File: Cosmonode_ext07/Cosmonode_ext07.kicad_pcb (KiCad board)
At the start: 2 copper layers, 37.5 x 34.3 mm, 9 parts, among them J1 OSHW_Logo, J2 MH-Z19, J3 CONN_01X08, J4 CONN_01X08, J5 GS3, J6 GS3, J7 Aloes_Logo, J8 CONN_01X09, U1 XC6206P502MR

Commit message: fully update to v0.3
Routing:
- net Net-(J2-Pad7): track 2.43 -> 46.7 mm, vias 1 -> 0
- net GND: track 49.2 -> 23.1 mm
- net +3V3: track 37.6 -> 44.6 mm
- net /TX: track 9.52 -> 11.0 mm
- net /AREF: track 27.8 -> 26.3 mm
- net +5V: track 21.7 -> 23.0 mm
- added copper zone on B.Cu, net GND
- added copper zone on F.Cu, net GND
- removed copper zone on B.Cu, net Net-(J2-Pad7)
- removed copper zone on F.Cu, net Net-(J2-Pad7)
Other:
- outline, holes or cut-outs redrawn

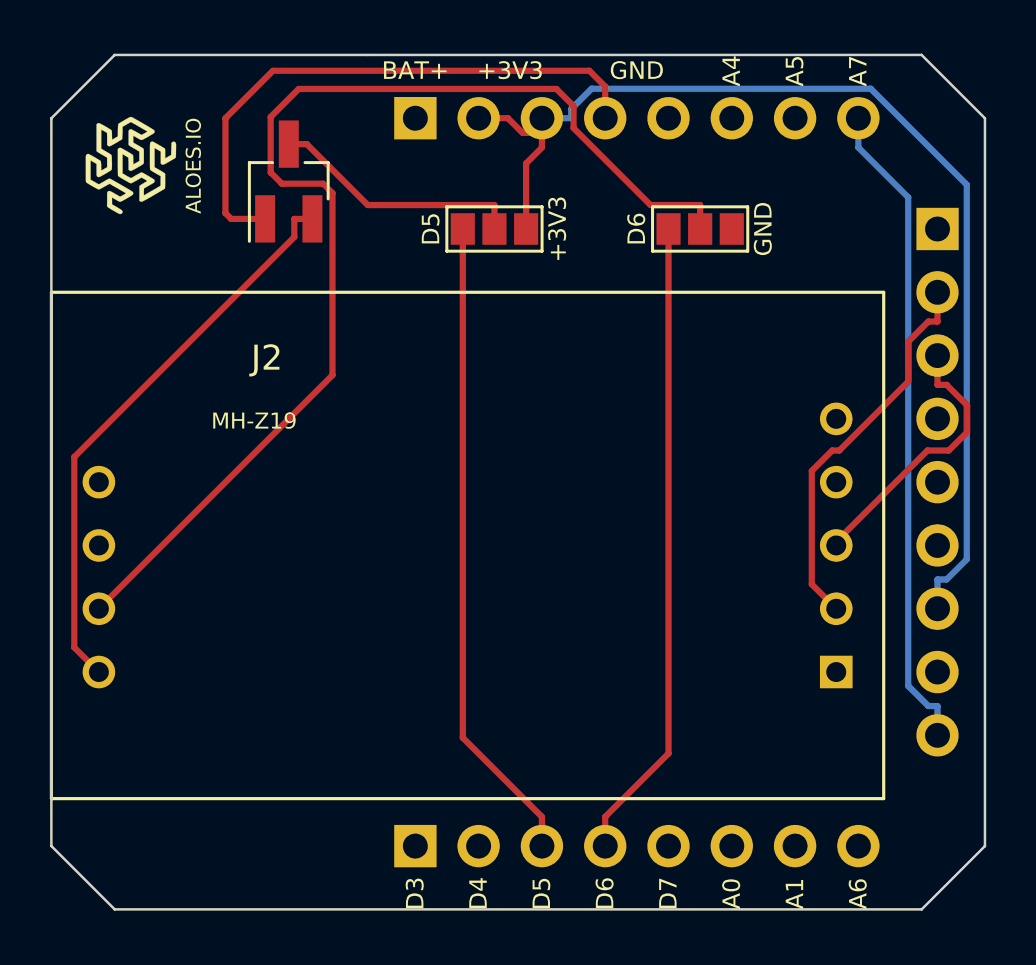
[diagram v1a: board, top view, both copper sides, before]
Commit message: update to v0.5 ( base, ext05, ext07, ext08 )
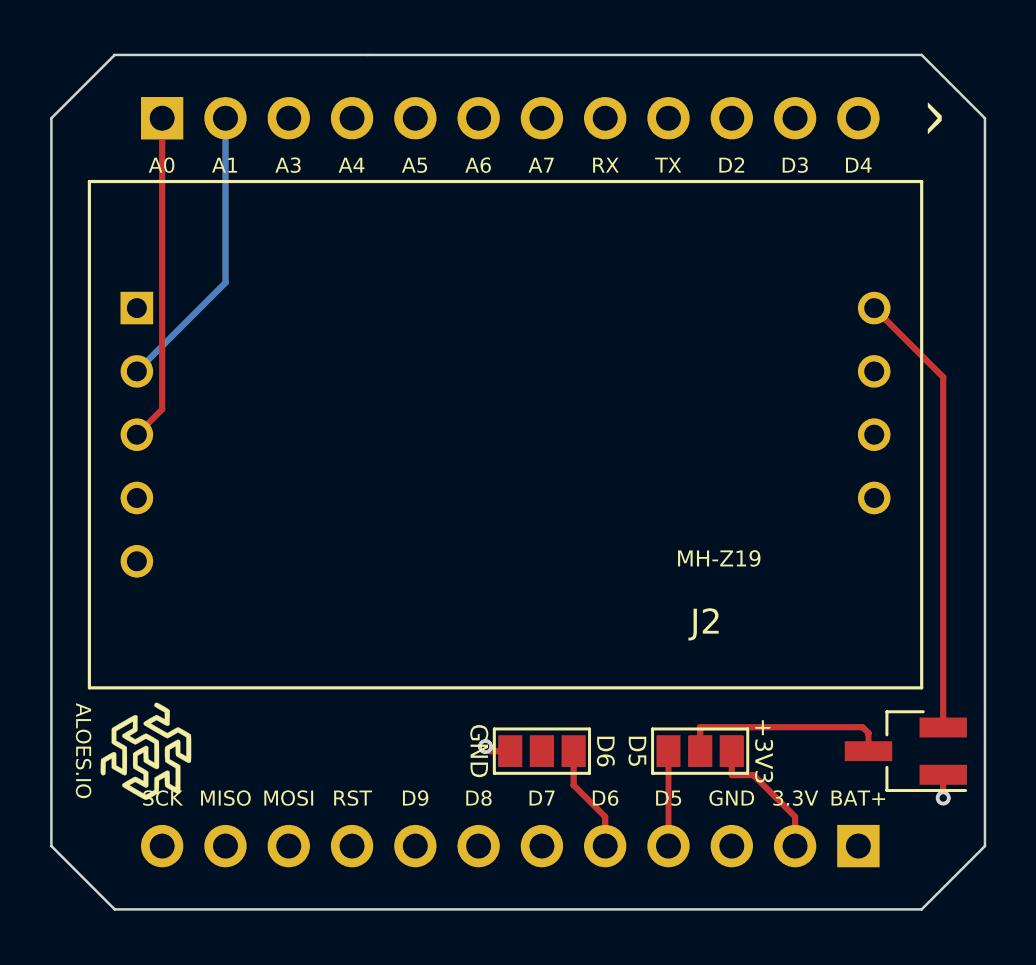
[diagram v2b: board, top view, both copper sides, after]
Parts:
- removed J8: CONN_01X09, Pin_Headers:Pin_Header_Straight_1x09_Pitch2.54mm
- J3, J4: value CONN_01X08 -> CONN_01X12; footprint Pin_Headers:Pin_Header_Straight_1x08_Pitch2.54mm -> Pin_Headers:Pin_Header_Straight_1x12_Pitch2.54mm
- moved J2 34.4 mm to (177.2, 99.1), turned to 180 degrees
- moved J4 34.2 mm to (176.5, 120.7), turned to 90 degrees
- moved U1 33.7 mm to (178.4, 116.8), turned to 180 degrees
- moved J3 30.9 mm to (148.6, 91.4)
- moved J7 23.5 mm to (148.0, 116.8), turned to 270 degrees
- moved J5 22.5 mm to (170.2, 116.8)
- moved J6 21.9 mm to (163.8, 116.8), turned to 270 degrees
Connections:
- net /A0 renamed A6
- net /A1 renamed A7
- net /A4 renamed D7
- net /A5 renamed D8
- net /A6 renamed RX
- net /BAT+ renamed +BATT
- net /D7 renamed A5
- J2 pad 2: /RX -> A1
- J2 pad 3: /TX -> A0
- J2 pad 7: Net-(J2-Pad7) -> GND
- J3 pad 1: /D3 -> A0
- J3 pad 2: /D4 -> A1
- J3 pad 3: /D5 -> A3
- J3 pad 4: /D6 -> A4
- J4 pad 3: +3V3 -> GND
- J4 pad 4: GND -> D5
- J4 pad 5: GND -> D6
- J4 pad 8: /AREF -> D9
- J5 pad 1: /D5 -> D5
- J6 pad 1: /D6 -> D6
- J6 pad 2: Net-(J2-Pad7) -> Net-(J6-Pad2)
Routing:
- net Net-(J2-Pad7): track 46.7 -> 0.00 mm
- net +3V3: track 44.6 -> 5.37 mm
- net /AREF: track 26.3 -> 0.00 mm
- net /D5: track 26.1 -> 0.00 mm
- net /D6: track 25.8 -> 0.00 mm
- net GND: track 23.1 -> 2.00 mm, vias 0 -> 2
- net /RX: track 15.6 -> 0.00 mm
- net A0: track 0.00 -> 13.1 mm
- net A1: track 0.00 -> 11.6 mm
- net /TX: track 11.0 -> 0.00 mm
- net +5V: track 23.0 -> 18.0 mm
- net D6: track 0.00 -> 4.34 mm
- net D5: track 0.00 -> 3.81 mm
- net Net-(J5-Pad2): track 10.2 -> 8.54 mm
- removed copper zone on F.Cu, net GND
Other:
- board text added: "3.3V"
- board text added: "A3"
- board text added: "D2"
- board text added: "D8"
- board text added: "D9"
- board text added: "MISO"
- board text added: "MOSI"
- board text added: "RST"
- board text added: "RX"
- board text added: "SCK"
- board text added: "TX"
- board text added: "^"

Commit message: update to V0.7 (WIP)
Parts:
- moved J7 2.01 mm to (149.9, 116.2)
- moved U1 2.01 mm to (176.5, 116.2)
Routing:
- net GND: track 2.00 -> 40.0 mm, vias 2 -> 0
- net Net-(J5-Pad2): track 8.54 -> 5.95 mm
- net Net-(J6-Pad2): track 0.00 -> 1.15 mm, vias 0 -> 1
- net +5V: track 18.0 -> 17.1 mm
- added copper zone on B.Cu, net Net-(J6-Pad2)
- removed copper zone on B.Cu, net GND
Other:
- board size 37.5 x 34.3 mm -> 34.3 x 34.3 mm
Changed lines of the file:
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@@
-(kicad_pcb (version 4) (host pcbnew 4.0.7-e2-6376~58~ubuntu17.04.1)
+(kicad_pcb (version 4) (host pcbnew 4.0.7-e2-6376~60~ubuntu17.10.1)
   (general
     (links 10)
     (no_connects 0)
-    (area 144.094999 88.849999 181.660001 123.240001)
+    (area 145.364999 88.849999 179.755001 123.240001)
     (thickness 1.6)
     (drawings 42)
-    (tracks 23)
+    (tracks 45)
     (zones 0)
     (modules 8)
@@
   )
   (module Aloes:Aloes_mini (layer F.Cu)
-    (at 147.955 116.84 270)
+    (at 149.86 116.205 270)
     (fp_text reference J7 (at 0 0 270) (layer F.SilkS) hide
       (effects (font (thickness 0.3)))
@@
   )
   (module TO_SOT_Packages_SMD:SOT-23_Handsoldering (layer F.Cu)
-    (at 178.435 116.84 180)
+    (at 176.53 116.205 180)
     (descr "SOT-23, Handsoldering")
     (tags SOT-23)
@@
     )
   )
-  (gr_text ^ (at 179.07 91.44 270) (layer F.SilkS)
+  (gr_line (start 147.955 123.19) (end 177.165 123.19) (angle 90) (layer Edge.Cuts) (width 0.1))
+  (gr_line (start 147.955 88.9) (end 156.845 88.9) (angle 90) (layer Edge.Cuts) (width 0.1))
+  (gr_line (start 145.415 120.65) (end 147.955 123.19) (angle 90) (layer Edge.Cuts) (width 0.1))
+  (gr_line (start 145.415 91.44) (end 145.415 120.65) (angle 90) (layer Edge.Cuts) (width 0.1))
+  (gr_line (start 147.955 88.9) (end 145.415 91.44) (angle 90) (layer Edge.Cuts) (width 0.1))
+  (gr_line (start 156.845 88.9) (end 177.165 88.9) (angle 90) (layer Edge.Cuts) (width 0.1))
+  (gr_line (start 179.705 91.44) (end 177.165 88.9) (angle 90) (layer Edge.Cuts) (width 0.1))
+  (gr_line (start 179.705 120.65) (end 179.705 91.44) (angle 90) (layer Edge.Cuts) (width 0.1))
+  (gr_line (start 177.165 123.19) (end 179.705 120.65) (angle 90) (layer Edge.Cuts) (width 0.1))
+  (gr_text ^ (at 177.8 91.44 270) (layer F.SilkS)
     (effects (font (size 1.5 1.5) (thickness 0.3)))
   )
@@
     (effects (font (size 0.6 0.6) (thickness 0.1)))
   )
-  (gr_line (start 179.07 123.19) (end 146.685 123.19) (angle 90) (layer Edge.Cuts) (width 0.1))
-  (gr_line (start 181.61 91.44) (end 181.61 120.65) (angle 90) (layer Edge.Cuts) (width 0.1))
-  (gr_line (start 156.845 88.9) (end 179.07 88.9) (angle 90) (layer Edge.Cuts) (width 0.1))
-  (gr_line (start 181.61 120.65) (end 179.07 123.19) (angle 90) (layer Edge.Cuts) (width 0.1))
-  (gr_line (start 179.07 88.9) (end 181.61 91.44) (angle 90) (layer Edge.Cuts) (width 0.1))
   (gr_text GND (at 161.29 116.84 270) (layer F.SilkS)
     (effects (font (size 0.7 0.7) (thickness 0.1)))
@@
     (effects (font (size 0.7 0.7) (thickness 0.1)) (justify mirror))
   )
-  (gr_line (start 146.685 88.9) (end 156.845 88.9) (angle 90) (layer Edge.Cuts) (width 0.1))
-  (gr_line (start 144.145 91.44) (end 146.685 88.9) (angle 90) (layer Edge.Cuts) (width 0.1))
-  (gr_line (start 144.145 120.65) (end 144.145 91.44) (angle 90) (layer Edge.Cuts) (width 0.1))
-  (gr_line (start 146.685 123.19) (end 144.145 120.65) (angle 90) (layer Edge.Cuts) (width 0.1))
   (dimension 24.13 (width 0.3) (layer F.Fab)
     (gr_text "24,130 mm" (at 166.37 79.295) (layer F.Fab)
@@
     (arrow2b (pts (xy 154.305 80.645) (xy 155.431504 80.058579)))
   )
-  (gr_text ALOES.IO (at 145.415 116.84 270) (layer F.SilkS)
+  (gr_text ALOES.IO (at 147.32 116.205 270) (layer F.SilkS)
     (effects (font (size 0.6 0.6) (thickness 0.1)))
   )
@@
     (arrow2b (pts (xy 188.595 89.535) (xy 189.181421 90.661504)))
   )
-  (segment (start 179.935 101.83) (end 177.165 99.06) (width 0.25) (layer F.Cu) (net 1))
-  (segment (start 179.935 115.89) (end 179.935 101.83) (width 0.25) (layer F.Cu) (net 1))
+  (segment (start 178.6386 100.5336) (end 177.165 99.06) (width 0.25) (layer F.Cu) (net 1))
+  (segment (start 178.6386 113.9211) (end 178.6386 100.5336) (width 0.25) (layer F.Cu) (net 1))
+  (segment (start 178.03 114.5297) (end 178.6386 113.9211) (width 0.25) (layer F.Cu) (net 1))
+  (segment (start 178.03 115.255) (end 178.03 114.5297) (width 0.25) (layer F.Cu) (net 1))
   (segment (start 172.3156 117.8003) (end 171.45 117.8003) (width 0.25) (layer F.Cu) (net 2))
   (segment (start 173.99 119.4747) (end 172.3156 117.8003) (width 0.25) (layer F.Cu) (net 2))
   (segment (start 173.99 120.65) (end 173.99 119.4747) (width 0.25) (layer F.Cu) (net 2))
   (segment (start 171.45 116.84) (end 171.45 117.8003) (width 0.25) (layer F.Cu) (net 2))
-  (via (at 179.935 118.7207) (size 0.6) (layers F.Cu B.Cu) (net 3))
-  (via (at 161.5658 116.6561) (size 0.6) (layers F.Cu B.Cu) (net 3))
-  (segment (start 179.935 118.7207) (end 179.935 117.79) (width 0.25) (layer F.Cu) (net 3))
-  (segment (start 162.56 116.84) (end 161.7497 116.84) (width 0.25) (layer F.Cu) (net 3))
-  (segment (start 161.5658 116.6561) (end 161.7497 116.84) (width 0.25) (layer F.Cu) (net 3))
-  (segment (start 176.7 115.8797) (end 170.18 115.8797) (width 0.25) (layer F.Cu) (net 4))
-  (segment (start 176.935 116.1147) (end 176.7 115.8797) (width 0.25) (layer F.Cu) (net 4))
-  (segment (start 176.935 116.84) (end 176.935 116.1147) (width 0.25) (layer F.Cu) (net 4))
+  (segment (start 175.3546 118.5551) (end 176.7547 117.155) (width 0.25) (layer F.Cu) (net 3))
+  (segment (start 175.3546 120.9818) (end 175.3546 118.5551) (width 0.25) (layer F.Cu) (net 3))
+  (segment (start 174.4656 121.8708) (end 175.3546 120.9818) (width 0.25) (layer F.Cu) (net 3))
+  (segment (start 173.4788 121.8708) (end 174.4656 121.8708) (width 0.25) (layer F.Cu) (net 3))
+  (segment (start 172.6253 121.0173) (end 173.4788 121.8708) (width 0.25) (layer F.Cu) (net 3))
+  (segment (start 172.6253 120.65) (end 172.6253 121.0173) (width 0.25) (layer F.Cu) (net 3))
+  (segment (start 172.0377 120.65) (end 172.6253 120.65) (width 0.25) (layer F.Cu) (net 3))
+  (segment (start 178.03 117.155) (end 176.8673 117.155) (width 0.25) (layer F.Cu) (net 3))
+  (segment (start 176.8673 117.155) (end 176.7547 117.155) (width 0.25) (layer F.Cu) (net 3))
+  (segment (start 178.1882 102.6232) (end 177.165 101.6) (width 0.25) (layer F.Cu) (net 3))
+  (segment (start 178.1882 108.8937) (end 178.1882 102.6232) (width 0.25) (layer F.Cu) (net 3))
+  (segment (start 176.7547 110.3272) (end 178.1882 108.8937) (width 0.25) (layer F.Cu) (net 3))
+  (segment (start 176.7547 117.155) (end 176.7547 110.3272) (width 0.25) (layer F.Cu) (net 3))
+  (segment (start 162.56 116.84) (end 162.56 117.8003) (width 0.25) (layer F.Cu) (net 3))
+  (segment (start 172.0377 120.65) (end 171.45 120.65) (width 0.25) (layer F.Cu) (net 3))
+  (segment (start 162.6455 117.8003) (end 162.56 117.8003) (width 0.25) (layer F.Cu) (net 3))
+  (segment (start 165.1002 120.255) (end 162.6455 117.8003) (width 0.25) (layer F.Cu) (net 3))
+  (segment (start 165.1002 121.0828) (end 165.1002 120.255) (width 0.25) (layer F.Cu) (net 3))
+  (segment (start 165.8659 121.8485) (end 165.1002 121.0828) (width 0.25) (layer F.Cu) (net 3))
+  (segment (start 169.4435 121.8485) (end 165.8659 121.8485) (width 0.25) (layer F.Cu) (net 3))
+  (segment (start 170.2747 121.0173) (end 169.4435 121.8485) (width 0.25) (layer F.Cu) (net 3))
+  (segment (start 170.2747 120.65) (end 170.2747 121.0173) (width 0.25) (layer F.Cu) (net 3))
+  (segment (start 171.45 120.65) (end 170.2747 120.65) (width 0.25) (layer F.Cu) (net 3))
+  (segment (start 173.4294 115.8797) (end 170.18 115.8797) (width 0.25) (layer F.Cu) (net 4))
+  (segment (start 173.7547 116.205) (end 173.4294 115.8797) (width 0.25) (layer F.Cu) (net 4))
+  (segment (start 175.03 116.205) (end 173.7547 116.205) (width 0.25) (layer F.Cu) (net 4))
   (segment (start 170.18 116.84) (end 170.18 115.8797) (width 0.25) (layer F.Cu) (net 4))
   (segment (start 151.13 98.044) (end 147.574 101.6) (width 0.25) (layer B.Cu) (net 10))
@@
   (segment (start 166.37 119.4747) (end 165.1 118.2047) (width 0.25) (layer F.Cu) (net 24))
   (segment (start 166.37 120.65) (end 166.37 119.4747) (width 0.25) (layer F.Cu) (net 24))
-  (zone (net 3) (net_name GND) (layer B.Cu) (hatch edge 0.508)
+  (via (at 163.83 115.6927) (size 0.6) (layers F.Cu B.Cu) (net 32))
+  (segment (start 163.83 115.6927) (end 163.83 116.84) (width 0.25) (layer F.Cu) (net 32))
+  (zone (net 32) (net_name "Net-(J6-Pad2)") (layer B.Cu) (hatch edge 0.508)
     (connect_pads (clearance 0.508))
     (min_thickness 0.254)
@@
     (polygon
       (pts
-        (xy 144.145 91.44) (xy 144.145 120.65) (xy 146.685 123.19) (xy 179.07 123.19) (xy 181.61 120.65)
-        (xy 181.61 91.44) (xy 179.07 88.9) (xy 146.685 88.9)
+        (xy 179.705 91.44) (xy 179.705 120.65) (xy 177.165 123.19) (xy 147.955 123.19) (xy 145.415 120.65)
+        (xy 145.415 91.44) (xy 147.955 88.9) (xy 177.165 88.9)
       )
     )
